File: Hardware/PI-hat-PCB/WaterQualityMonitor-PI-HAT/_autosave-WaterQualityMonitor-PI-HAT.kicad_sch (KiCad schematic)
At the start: 29 parts

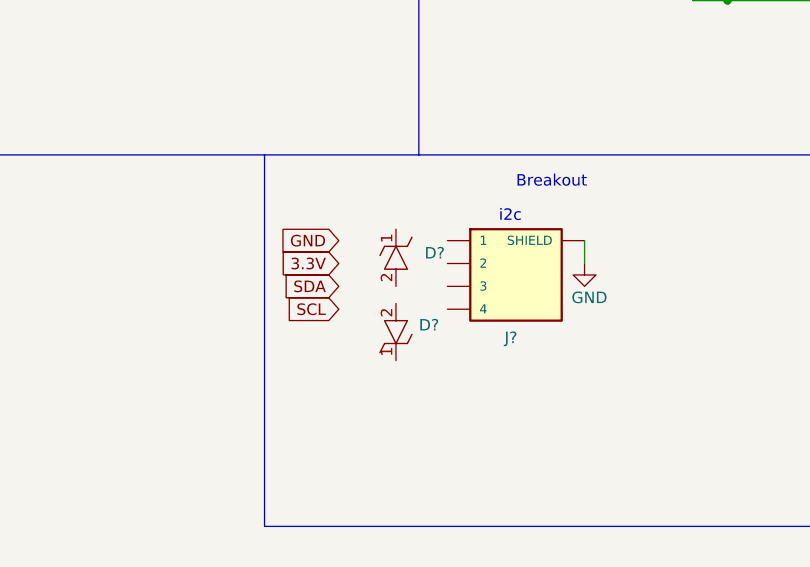
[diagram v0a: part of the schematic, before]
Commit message: documentation and schematic improvements
documentation updated, design choices update on led driver
added esd protection options diodes and ic for i2c esd protection
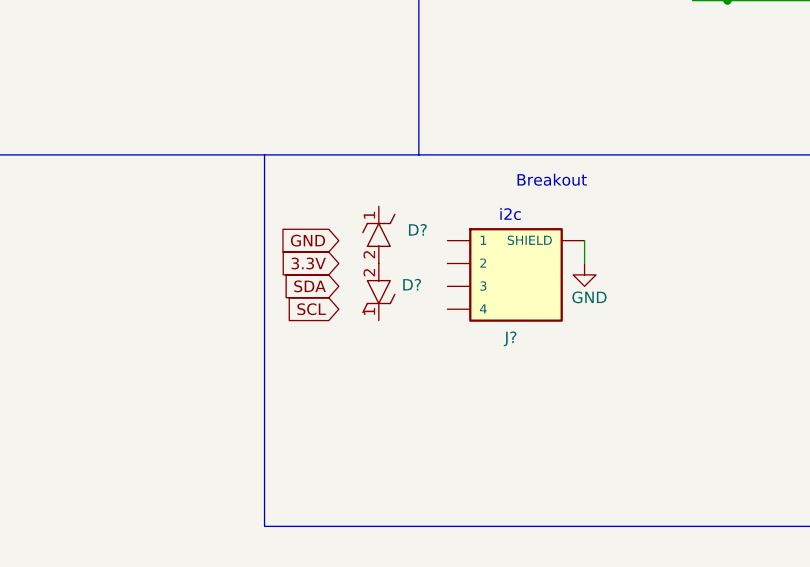
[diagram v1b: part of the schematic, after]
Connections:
- net at D?.2: now also D?.2
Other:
- moved on the sheet: D?
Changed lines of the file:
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@@
     (pin "2")
   )
-  (symbol (lib_name "VESD01C1-02V-G3-08_1") (lib_id "SamacSys_Parts:VESD01C1-02V-G3-08") (at 179.705 76.2 270) (unit 1)
-    (in_bom yes) (on_board yes) (fields_autoplaced)
-    (property "Reference" "D?" (id 0) (at 182.88 83.3119 90)
-      (effects (font (size 1.27 1.27)) (justify left))
-    )
-    (property "Value" "VESD01C1-02V-G3-08" (id 1) (at 182.88 85.217 90)
+  (symbol (lib_name "VESD01C1-02V-G3-08_1") (lib_id "SamacSys_Parts:VESD01C1-02V-G3-08") (at 177.8 73.66 270) (unit 1)
+    (in_bom yes) (on_board yes) (fields_autoplaced)
+    (property "Reference" "D?" (id 0) (at 180.975 80.7719 90)
+      (effects (font (size 1.27 1.27)) (justify left))
+    )
+    (property "Value" "VESD01C1-02V-G3-08" (id 1) (at 180.975 82.677 90)
       (effects (font (size 1 1)) (justify left) hide)
     )
-    (property "Footprint" "SODFL1608X70N" (id 2) (at 169.545 80.01 0)
-      (effects (font (size 1.27 1.27)) (justify left bottom) hide)
-    )
-    (property "Datasheet" "https://www.mouser.in/datasheet/2/427/vesd01c1-02vtovesd33c1-02v-1767831.pdf" (id 3) (at 169.545 77.47 0)
-      (effects (font (size 1.27 1.27)) (justify left bottom) hide)
-    )
-    (property "Description" "ESD Suppressors / TVS Diodes 1 V Unidirectional SOD-523" (id 4) (at 169.545 74.93 0)
-      (effects (font (size 1.27 1.27)) (justify left bottom) hide)
-    )
-    (property "Height" "0.7" (id 5) (at 169.545 72.39 0)
-      (effects (font (size 1.27 1.27)) (justify left bottom) hide)
-    )
-    (property "Mouser Part Number" "78-VESD01C1-02V-G308" (id 6) (at 169.545 69.85 0)
-      (effects (font (size 1.27 1.27)) (justify left bottom) hide)
-    )
-    (property "Mouser Price/Stock" "https://www.mouser.co.uk/ProductDetail/Vishay-Semiconductors/VESD01C1-02V-G3-08?qs=ds50AKTGxA%252BgIwLx7rxquQ%3D%3D" (id 7) (at 169.545 67.31 0)
-      (effects (font (size 1.27 1.27)) (justify left bottom) hide)
-    )
-    (property "Manufacturer_Name" "Vishay" (id 8) (at 169.545 64.77 0)
-      (effects (font (size 1.27 1.27)) (justify left bottom) hide)
-    )
-    (property "Manufacturer_Part_Number" "VESD01C1-02V-G3-08" (id 9) (at 169.545 62.23 0)
-      (effects (font (size 1.27 1.27)) (justify left bottom) hide)
-    )
-    (property "Purpose" "ESD suppresion" (id 10) (at 179.705 76.2 0)
+    (property "Footprint" "SODFL1608X70N" (id 2) (at 167.64 77.47 0)
+      (effects (font (size 1.27 1.27)) (justify left bottom) hide)
+    )
+    (property "Datasheet" "https://www.mouser.in/datasheet/2/427/vesd01c1-02vtovesd33c1-02v-1767831.pdf" (id 3) (at 167.64 74.93 0)
+      (effects (font (size 1.27 1.27)) (justify left bottom) hide)
+    )
+    (property "Description" "ESD Suppressors / TVS Diodes 1 V Unidirectional SOD-523" (id 4) (at 167.64 72.39 0)
+      (effects (font (size 1.27 1.27)) (justify left bottom) hide)
+    )
+    (property "Height" "0.7" (id 5) (at 167.64 69.85 0)
+      (effects (font (size 1.27 1.27)) (justify left bottom) hide)
+    )
+    (property "Mouser Part Number" "78-VESD01C1-02V-G308" (id 6) (at 167.64 67.31 0)
+      (effects (font (size 1.27 1.27)) (justify left bottom) hide)
+    )
+    (property "Mouser Price/Stock" "https://www.mouser.co.uk/ProductDetail/Vishay-Semiconductors/VESD01C1-02V-G3-08?qs=ds50AKTGxA%252BgIwLx7rxquQ%3D%3D" (id 7) (at 167.64 64.77 0)
+      (effects (font (size 1.27 1.27)) (justify left bottom) hide)
+    )
+    (property "Manufacturer_Name" "Vishay" (id 8) (at 167.64 62.23 0)
+      (effects (font (size 1.27 1.27)) (justify left bottom) hide)
+    )
+    (property "Manufacturer_Part_Number" "VESD01C1-02V-G3-08" (id 9) (at 167.64 59.69 0)
+      (effects (font (size 1.27 1.27)) (justify left bottom) hide)
+    )
+    (property "Purpose" "ESD suppresion" (id 10) (at 177.8 73.66 0)
       (effects (font (size 1.27 1.27)) hide)
     )
@@
     (pin "1")
   )
-  (symbol (lib_name "VESD01C1-02V-G3-08_1") (lib_id "SamacSys_Parts:VESD01C1-02V-G3-08") (at 179.705 99.695 90) (unit 1)
-    (in_bom yes) (on_board yes) (fields_autoplaced)
-    (property "Reference" "D?" (id 0) (at 182.245 91.3129 90)
+  (symbol (lib_name "VESD01C1-02V-G3-08_1") (lib_id "SamacSys_Parts:VESD01C1-02V-G3-08") (at 177.8 95.25 90) (unit 1)
+    (in_bom yes) (on_board yes) (fields_autoplaced)
+    (property "Reference" "D?" (id 0) (at 180.34 86.8679 90)
       (effects (font (size 1.27 1.27)) (justify right))
     )
-    (property "Value" "VESD01C1-02V-G3-08" (id 1) (at 176.53 90.678 90)
+    (property "Value" "VESD01C1-02V-G3-08" (id 1) (at 174.625 86.233 90)
       (effects (font (size 1 1)) (justify left) hide)
     )
-    (property "Footprint" "SODFL1608X70N" (id 2) (at 189.865 95.885 0)
-      (effects (font (size 1.27 1.27)) (justify left bottom) hide)
-    )
-    (property "Datasheet" "https://www.mouser.in/datasheet/2/427/vesd01c1-02vtovesd33c1-02v-1767831.pdf" (id 3) (at 189.865 98.425 0)
-      (effects (font (size 1.27 1.27)) (justify left bottom) hide)
-    )
-    (property "Description" "ESD Suppressors / TVS Diodes 1 V Unidirectional SOD-523" (id 4) (at 189.865 100.965 0)
-      (effects (font (size 1.27 1.27)) (justify left bottom) hide)
-    )
-    (property "Height" "0.7" (id 5) (at 189.865 103.505 0)
-      (effects (font (size 1.27 1.27)) (justify left bottom) hide)
-    )
-    (property "Mouser Part Number" "78-VESD01C1-02V-G308" (id 6) (at 189.865 106.045 0)
-      (effects (font (size 1.27 1.27)) (justify left bottom) hide)
-    )
-    (property "Mouser Price/Stock" "https://www.mouser.co.uk/ProductDetail/Vishay-Semiconductors/VESD01C1-02V-G3-08?qs=ds50AKTGxA%252BgIwLx7rxquQ%3D%3D" (id 7) (at 189.865 108.585 0)
-      (effects (font (size 1.27 1.27)) (justify left bottom) hide)
-    )
-    (property "Manufacturer_Name" "Vishay" (id 8) (at 189.865 111.125 0)
-      (effects (font (size 1.27 1.27)) (justify left bottom) hide)
-    )
-    (property "Manufacturer_Part_Number" "VESD01C1-02V-G3-08" (id 9) (at 189.865 113.665 0)
-      (effects (font (size 1.27 1.27)) (justify left bottom) hide)
-    )
-    (property "Purpose" "ESD suppresion" (id 10) (at 182.245 93.8529 90)
+    (property "Footprint" "SODFL1608X70N" (id 2) (at 187.96 91.44 0)
+      (effects (font (size 1.27 1.27)) (justify left bottom) hide)
+    )
+    (property "Datasheet" "https://www.mouser.in/datasheet/2/427/vesd01c1-02vtovesd33c1-02v-1767831.pdf" (id 3) (at 187.96 93.98 0)
+      (effects (font (size 1.27 1.27)) (justify left bottom) hide)
+    )
+    (property "Description" "ESD Suppressors / TVS Diodes 1 V Unidirectional SOD-523" (id 4) (at 187.96 96.52 0)
+      (effects (font (size 1.27 1.27)) (justify left bottom) hide)
+    )
+    (property "Height" "0.7" (id 5) (at 187.96 99.06 0)
+      (effects (font (size 1.27 1.27)) (justify left bottom) hide)
+    )
+    (property "Mouser Part Number" "78-VESD01C1-02V-G308" (id 6) (at 187.96 101.6 0)
+      (effects (font (size 1.27 1.27)) (justify left bottom) hide)
+    )
+    (property "Mouser Price/Stock" "https://www.mouser.co.uk/ProductDetail/Vishay-Semiconductors/VESD01C1-02V-G3-08?qs=ds50AKTGxA%252BgIwLx7rxquQ%3D%3D" (id 7) (at 187.96 104.14 0)
+      (effects (font (size 1.27 1.27)) (justify left bottom) hide)
+    )
+    (property "Manufacturer_Name" "Vishay" (id 8) (at 187.96 106.68 0)
+      (effects (font (size 1.27 1.27)) (justify left bottom) hide)
+    )
+    (property "Manufacturer_Part_Number" "VESD01C1-02V-G3-08" (id 9) (at 187.96 109.22 0)
+      (effects (font (size 1.27 1.27)) (justify left bottom) hide)
+    )
+    (property "Purpose" "ESD suppresion" (id 10) (at 180.34 89.4079 90)
       (effects (font (size 1.27 1.27)) (justify right) hide)
     )
